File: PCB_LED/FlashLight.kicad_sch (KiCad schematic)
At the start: 49 parts, among them J1 USB_C_Receptacle_USB2.0_16P, J2 Conn_01x01_Pin, J3 Conn_01x02, K2 HEADER_MALE_1X1, K3 HEADER_MALE_1X1, K5 HEADER_MALE_1X1, K6 HEADER_MALE_1X1, K8 HEADER_MALE_1X1, K9 HEADER_MALE_1X1, Q1 DMG9926UDM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

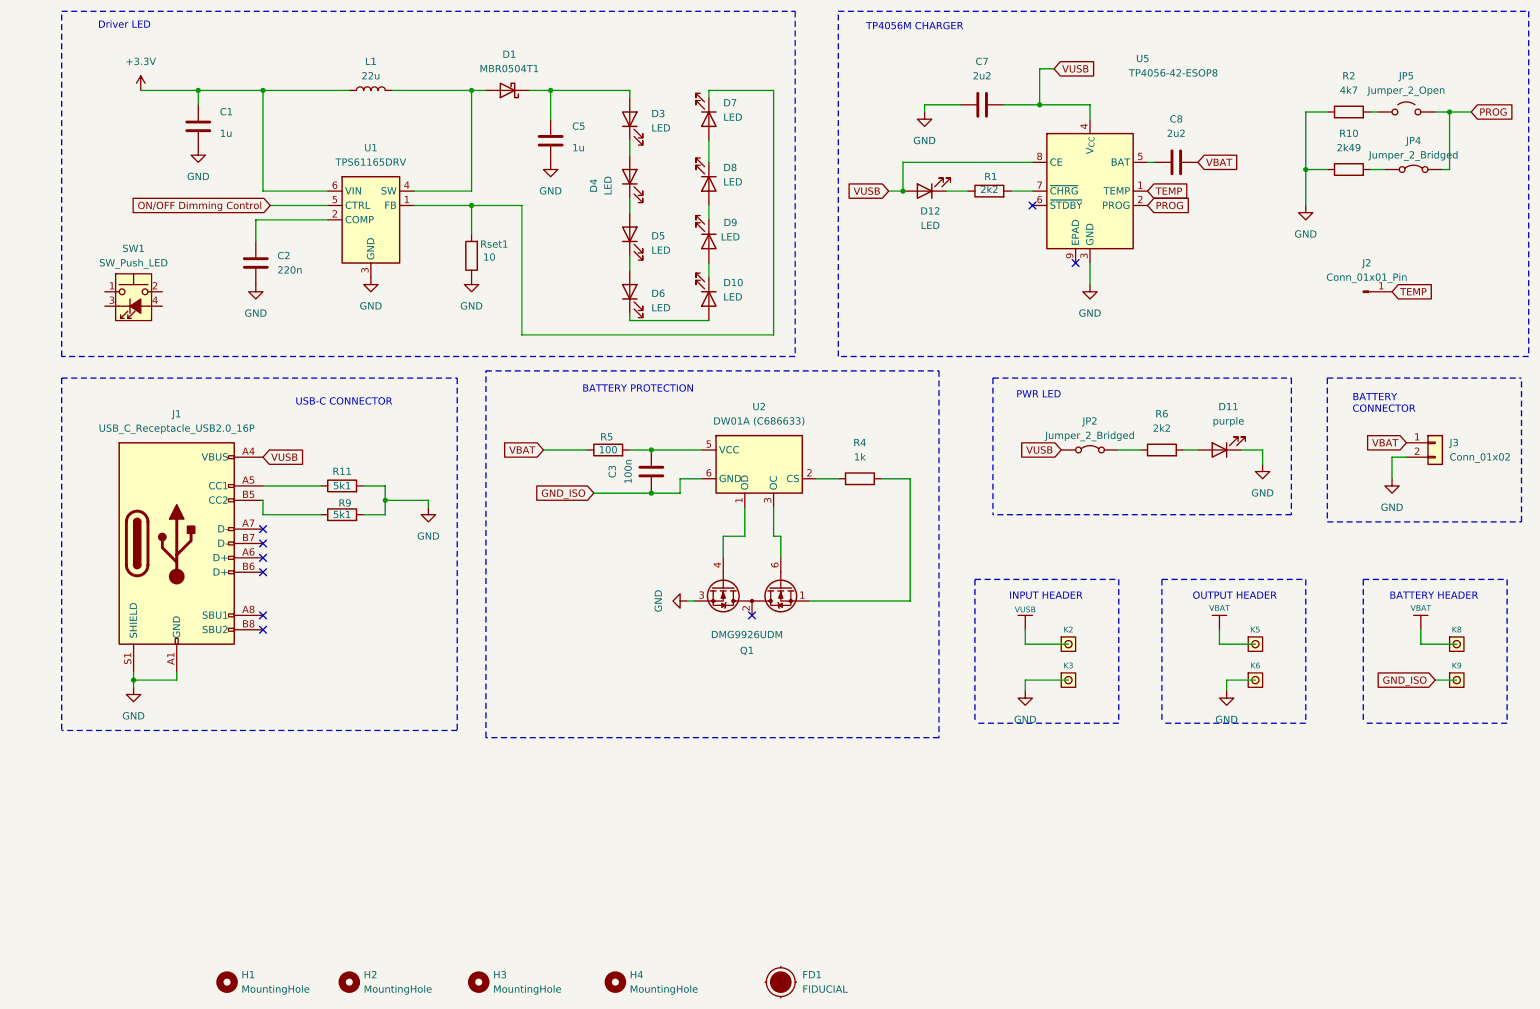
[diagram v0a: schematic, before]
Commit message: Driver TI
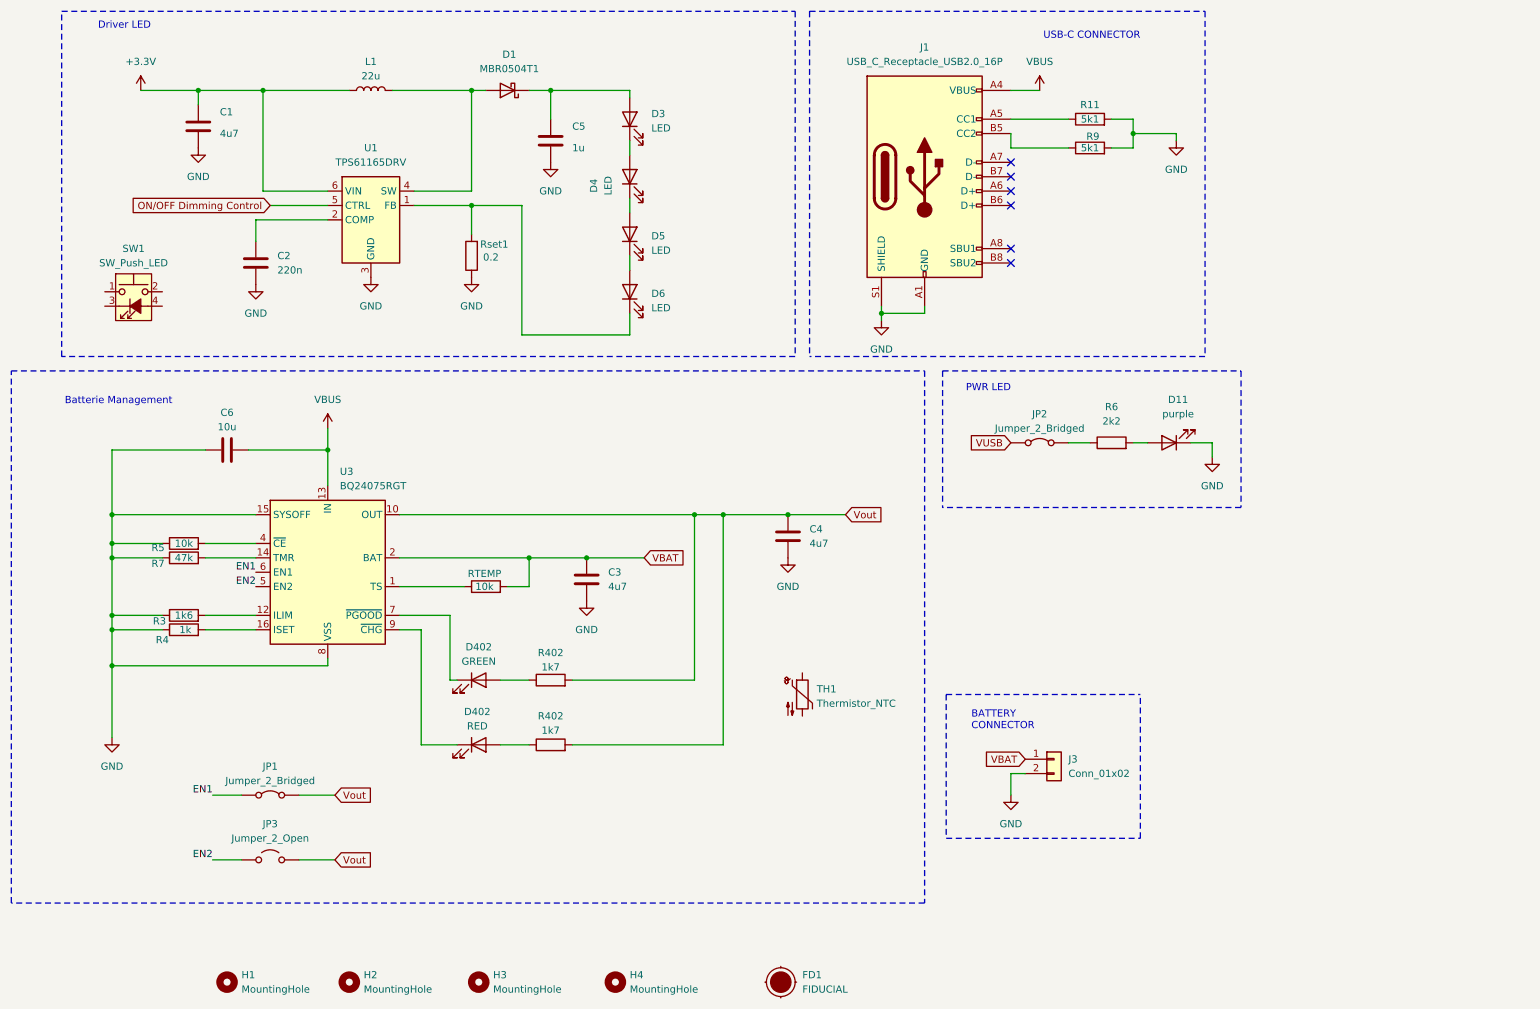
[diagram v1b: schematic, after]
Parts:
- removed C7, C8: 2u2, symbol Device:C
- removed D10, D12, D7, D8, D9: LED, symbol Device:LED
- removed J2: Conn_01x01_Pin, Connector_PinHeader_2.54mm:PinHeader_1x01_P2.54mm_Vertical, symbol Connector:Conn_01x01_Pin
- removed JP4: Jumper_2_Bridged, symbol Jumper:Jumper_2_Bridged
- removed JP5: Jumper_2_Open, symbol Jumper:Jumper_2_Open
- removed K2, K3, K5, K6, K9: HEADER_MALE_1X1, Connector_PinHeader_2.00mm:PinHeader_1x01_P2.00mm_Vertical, symbol e-radionica.com schematics:HEADER_MALE_1X1
- removed K8: HEADER_MALE_1X1, Connector_PinHeader_2.00mm:PinHeader_1x01_P2.00mm_Horizontal, symbol e-radionica.com schematics:HEADER_MALE_1X1
- removed Q1: DMG9926UDM, Package_TO_SOT_SMD:SOT-23-6, symbol Transistor_FET:DMG9926UDM
- removed R1: 2k2, symbol Device:R
- removed R10: 2k49, symbol Device:R
- removed R2: 4k7, symbol Device:R
- removed U2: DW01A (C686633), Package_TO_SOT_SMD:SOT-23-6, symbol Battery_Management:DW01A
- removed U5: TP4056-42-ESOP8, Package_SO:SOIC-8-1EP_3.9x4.9mm_P1.27mm_EP2.41x3.3mm_ThermalVias, symbol Battery_Management:TP4056-42-ESOP8
- added C4: 4u7, symbol Device:C
- added C6: 10u, symbol Device:C
- added D402: GREEN, symbol Device:LED
- added D402: RED, symbol Device:LED
- added JP1: Jumper_2_Bridged, symbol Jumper:Jumper_2_Bridged
- added JP3: Jumper_2_Open, symbol Jumper:Jumper_2_Open
- added R3: 1k6, symbol Device:R
- added R402 (x2): 1k7, symbol Device:R
- added R7: 47k, symbol Device:R
- added RTEMP: 10k, symbol Device:R
- added TH1: Thermistor_NTC, symbol Device:Thermistor_NTC
- added U3: BQ24075RGT, Package_DFN_QFN:VQFN-16-1EP_3x3mm_P0.5mm_EP1.6x1.6mm, symbol Battery_Management:BQ24075RGT
- C1: value 1u -> 4u7
- C3: value 100n -> 4u7
- R5: value 100 -> 10k
- Rset1: value 10 -> 0.2
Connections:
- net GND_ISO is gone; now on net GND: C3.2
- net GND: now also R4.1, R5.1, C4.2, C6.1, R3.1, R7.1, U3.15 (SYSOFF), U3.17 (VSS), U3.8 (VSS)
- net VBAT: now also C3.1, RTEMP.2, U3.2 (BAT), U3.3 (BAT); no longer R5.1
- net VUSB: no longer J1.A4 (VBUS), J1.A9 (VBUS), J1.B4 (VBUS), J1.B9 (VBUS)
- net at Rset1.2, U1.1 (FB): now also D6.1 (K)
- net at R5.2: now also U3.4 (~{CE}); no longer C3.1
- net at R4.2: now also U3.16 (ISET)
- new net: RTEMP.1, U3.1 (TS)
- new net: R3.2, U3.12 (ILIM)
- new net: R7.2, U3.14 (TMR)
- new net: D402.1 (K), U3.7 (~{PGOOD})
- new net: D402.1 (K), U3.9 (~{CHG})
- new net: D402.2 (A), R402.1 (x2)
- new net EN1: JP1.1 (A), U3.6 (EN1)
- new net EN2: JP3.1 (A), U3.5 (EN2)
- new net VBUS: C6.2, J1.A4 (VBUS), J1.A9 (VBUS), J1.B4 (VBUS), J1.B9 (VBUS), U3.13 (IN)
- new net Vout: C4.1, JP1.2 (B), JP3.2 (B), R402.2, R402.2, U3.10 (OUT), U3.11 (OUT)
- no-connect marks 9 -> 6
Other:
- note added: "Batterie Management"
- note removed: "BATTERY HEADER"
- note removed: "BATTERY PROTECTION"
- note removed: "INPUT HEADER"
- note removed: "OUTPUT HEADER"
- note removed: "TP4056M CHARGER"
- moved on the sheet: D11, J1, J3, JP2, R11, R6, R9

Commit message: Modif 1
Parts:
- removed C3: 4u7, symbol Device:C
- removed FD1: FIDUCIAL, Fiducial:Fiducial_0.75mm_Mask2.25mm, symbol e-radionica.com schematics:FIDUCIAL
- removed H1, H2, H3, H4: MountingHole, MountingHole:MountingHole_3.2mm_M3, symbol Mechanical:MountingHole
- removed JP1: Jumper_2_Bridged, symbol Jumper:Jumper_2_Bridged
- removed JP3: Jumper_2_Open, symbol Jumper:Jumper_2_Open
- removed RTEMP: 10k, symbol Device:R
- removed SW1: SW_Push_LED, symbol Switch:SW_Push_LED
- removed TH1: Thermistor_NTC, symbol Device:Thermistor_NTC
- added H1, H2, H3, H4: MountingHole_Pad, symbol Mechanical:MountingHole_Pad
- added R1: 10k, symbol Device:R
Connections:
- net EN2 is gone; now on net GND: U3.5 (EN2)
- net ON/OFF Dimming Control is gone; now on net Vout: U1.5 (CTRL)
- net GND: now also H1.1, H2.1, H3.1, H4.1
- net VBUS: now also R1.1
- net Thermis: now reaches U3.1 (TS)
- net EN1: no longer names the net of U3.6 (EN1)
- net EN1: now also R1.2
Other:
- moved on the sheet: C4, D402, J3, R402

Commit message: Layout
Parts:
- removed C4: 4u7, symbol Device:C
- added C6: 4u7, Capacitor_SMD:C_0603_1608Metric_Pad1.08x0.95mm_HandSolder, symbol Device:C
- added SW1: SW_Push, Button_Switch_THT:SW_PUSH_6mm, symbol Switch:SW_Push
- added TH1: 10k, Resistor_SMD:R_0603_1608Metric_Pad0.98x0.95mm_HandSolder, symbol Device:Thermistor
- C2: renamed from C6; footprint (none) -> Capacitor_SMD:C_0603_1608Metric_Pad1.08x0.95mm_HandSolder
- D1, D2: renamed from D402; footprint (none) -> Diode_SMD:D_0603_1608Metric_Pad1.05x0.95mm_HandSolder
- D4: renamed from D3; footprint (none) -> LED_SMD:LED_Cree-XP
- D5: renamed from D4; footprint (none) -> LED_SMD:LED_Cree-XP
- D6: renamed from D5; footprint (none) -> LED_SMD:LED_Cree-XP
- D7: renamed from D6; footprint (none) -> LED_SMD:LED_Cree-XP
- D8: renamed from D11; value purple -> BLUE; footprint (none) -> LED_SMD:LED_0603_1608Metric_Pad1.05x0.95mm_HandSolder
- H1: renamed from H4; footprint (none) -> MountingHole:MountingHole_2.2mm_M2_DIN965_Pad
- H2: renamed from H3; footprint (none) -> MountingHole:MountingHole_2.2mm_M2_DIN965_Pad
- H3: renamed from H2; footprint (none) -> MountingHole:MountingHole_2.2mm_M2_DIN965_Pad
- H4: renamed from H1; footprint (none) -> MountingHole:MountingHole_2.2mm_M2_DIN965_Pad
- JP1: renamed from JP2; footprint (none) -> Jumper:SolderJumper-2_P1.3mm_Open_Pad1.0x1.5mm
- L1: value 22u -> 10u; footprint Inductor_SMD:L_0603_1608Metric_Pad1.05x0.95mm_HandSolder -> Inductor_SMD:L_Wuerth_WE-PD-Typ-7345
- R1, R9: footprint (none) -> Resistor_SMD:R_0402_1005Metric_Pad0.72x0.64mm_HandSolder
- R10: renamed from R6; footprint (none) -> Resistor_SMD:R_0402_1005Metric_Pad0.72x0.64mm_HandSolder
- R2: renamed from R5; footprint (none) -> Resistor_SMD:R_0402_1005Metric_Pad0.72x0.64mm_HandSolder
- R3: renamed from R7; footprint (none) -> Resistor_SMD:R_0402_1005Metric_Pad0.72x0.64mm_HandSolder
- R4: renamed from R3; value 1k6 -> 820; footprint (none) -> Resistor_SMD:R_0402_1005Metric_Pad0.72x0.64mm_HandSolder
- R5: renamed from R4; value 1k -> 910; footprint (none) -> Resistor_SMD:R_0402_1005Metric_Pad0.72x0.64mm_HandSolder
- R6: renamed from R402; value 1k7 -> 470; footprint (none) -> Resistor_SMD:R_0402_1005Metric_Pad0.72x0.64mm_HandSolder
- R7: renamed from R402; value 1k7 -> 680; footprint (none) -> Resistor_SMD:R_0402_1005Metric_Pad0.72x0.64mm_HandSolder
- R8: renamed from R11; footprint (none) -> Resistor_SMD:R_0402_1005Metric_Pad0.72x0.64mm_HandSolder
- Rset1: value 0.2 -> 0.27; footprint Resistor_SMD:R_0603_1608Metric_Pad0.98x0.95mm_HandSolder -> Resistor_SMD:R_0402_1005Metric_Pad0.72x0.64mm_HandSolder
- renumbered C2 to C3, C5 to C4, D1 to D3, J3 to J2, U3 to U1, U1 to U2
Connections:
- net +3.3V is gone; now on net Vout: C1.1, L1.1, U2.6 (VIN)
- net VUSB is gone; now on net VBUS: JP1.1 (A)
- net GND: now also U1.6 (EN1), C6.1, TH1.2; no longer U1.5 (EN2)
- net VBAT: now also C6.2
- net Vout: now also SW1.1; no longer U2.5 (CTRL)
- net at R1.2: now also U1.5 (EN2); no longer U1.6 (EN1)
- net Thermis: no longer names the net of U1.1 (TS)
- net Thermis: now also TH1.1
- new net: SW1.2, U2.5 (CTRL)
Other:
- moved on the sheet: C1, C2, C3, C4, D1, D2, D3, D4, D5, D6, D7, D8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
